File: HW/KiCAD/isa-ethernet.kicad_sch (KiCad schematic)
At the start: 42 parts, among them IC1 RTL8019AS, J5 IO-ADDR, J6 CONFIG, J7 CONFIG, J8 RJ45_LED_Shielded, U5 93LCxxB, Y2 20MHz

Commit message: some edit
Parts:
- IC1: footprint RTL8019AS:RTL8019AS -> Library:RTL8019AS
- J8: footprint Connector_RJ:RJ45_Bel_SI-60062-F -> Connector_RJ:RJ45_Cetus_J1B1211CCD_Horizontal
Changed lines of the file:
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@@
 			)
 		)
-		(property "Footprint" "Connector_RJ:RJ45_Bel_SI-60062-F"
+		(property "Footprint" "Connector_RJ:RJ45_Cetus_J1B1211CCD_Horizontal"
 			(at 259.08 33.655 90)
 			(effects
@@
 			)
 		)
-		(property "Footprint" "RTL8019AS:RTL8019AS"
+		(property "Footprint" "Library:RTL8019AS"
 			(at 152.4 101.6 0)
 			(effects

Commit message: some eidts, remove com
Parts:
- IC1: footprint Library:RTL8019AS -> kharon:RTL8019AS
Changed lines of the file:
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@@
 			)
 		)
-		(property "Footprint" "Library:RTL8019AS"
+		(property "Footprint" "kharon:RTL8019AS"
 			(at 152.4 101.6 0)
 			(effects

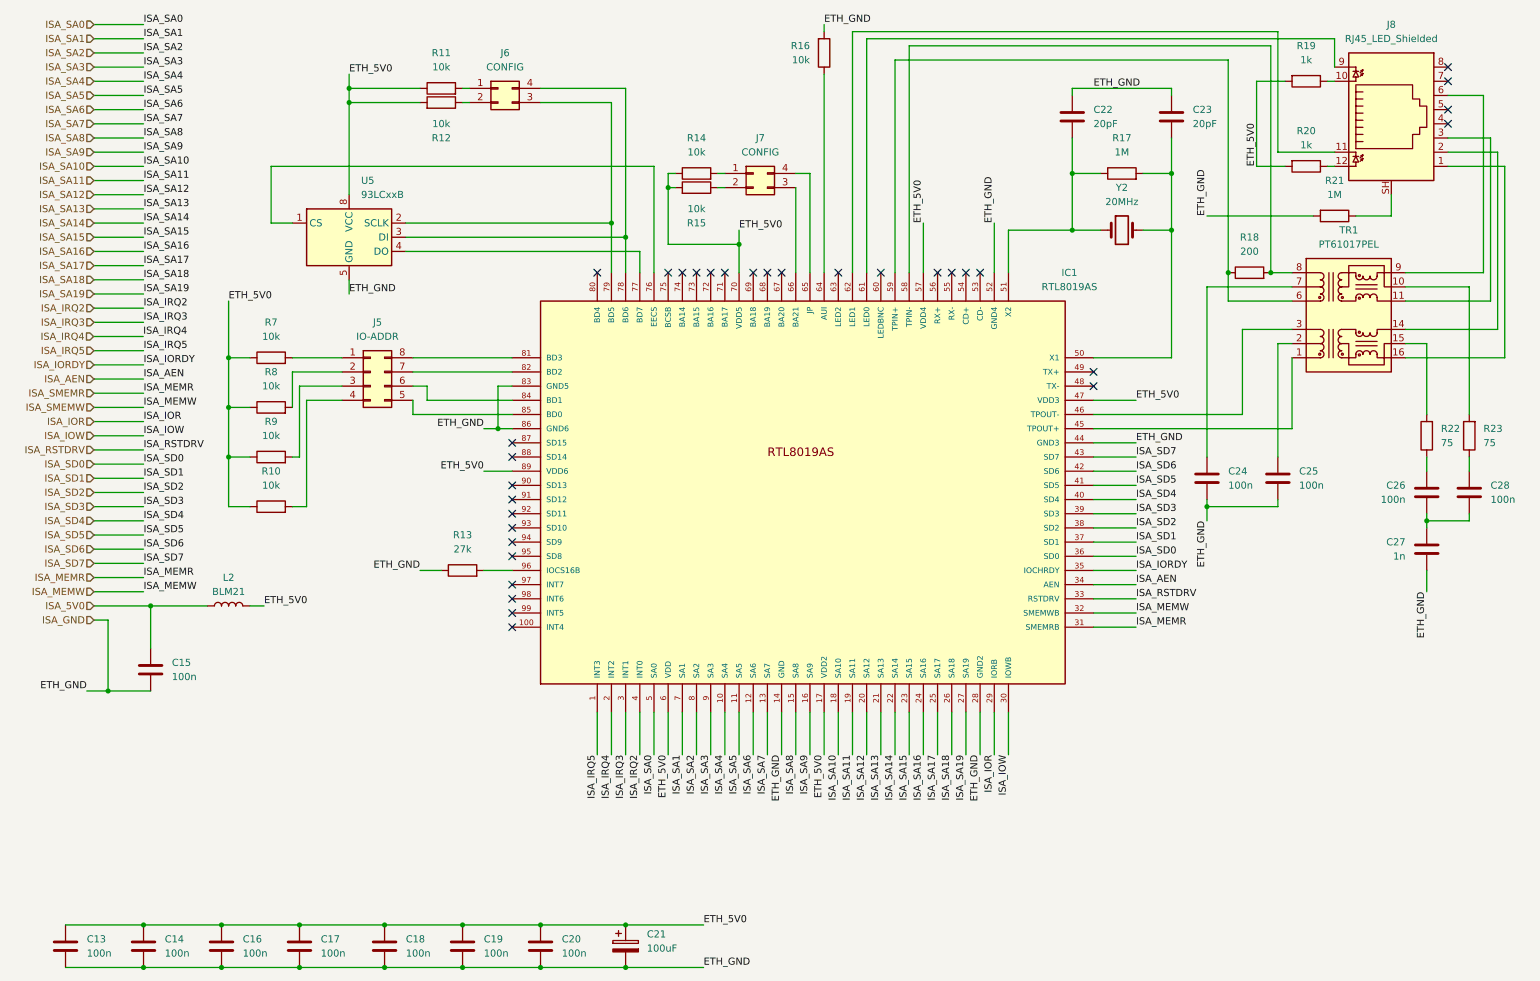
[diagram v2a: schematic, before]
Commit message: some edits, add HP amp
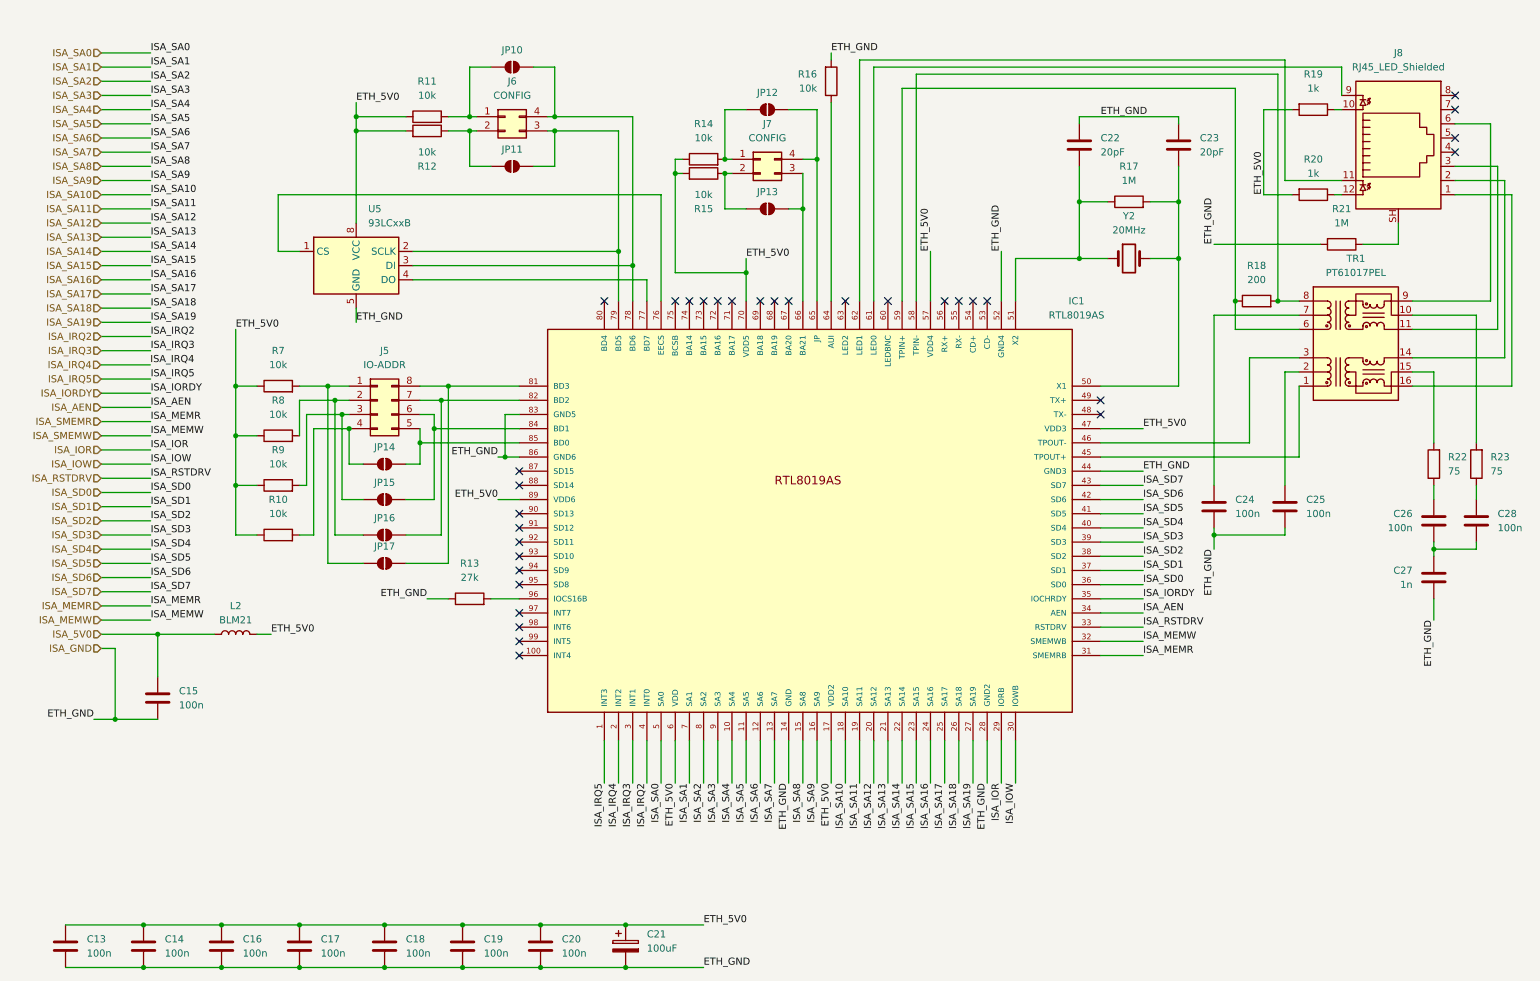
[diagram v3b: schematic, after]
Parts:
- added JP10, JP11, JP12, JP13, JP14, JP15, JP16, JP17: ~, Jumper:SolderJumper-2_P1.3mm_Open_TrianglePad1.0x1.5mm, symbol Jumper:SolderJumper_2_Open
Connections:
- net at J5.1 (Pin_1), R7.2: now also JP17.1 (A)
- net at J5.2 (Pin_2), R8.2: now also JP16.1 (A)
- net at J5.3 (Pin_3), R9.2: now also JP15.1 (A)
- net at J5.4 (Pin_4), R10.2: now also JP14.1 (A)
- net at IC1.85 (BD0), J5.5 (Pin_5): now also JP14.2 (B)
- net at IC1.84 (BD1), J5.6 (Pin_6): now also JP15.2 (B)
- net at IC1.82 (BD2), J5.7 (Pin_7): now also JP16.2 (B)
- net at IC1.81 (BD3), J5.8 (Pin_8): now also JP17.2 (B)
- net at J6.1 (Pin_1), R11.2: now also JP10.1 (A)
- net at J6.2 (Pin_2), R12.1: now also JP11.1 (A)
- net at IC1.79 (BD5), J6.3 (Pin_3), U5.2 (SCLK): now also JP11.2 (B)
- net at IC1.78 (BD6), J6.4 (Pin_4), U5.3 (DI): now also JP10.2 (B)
- net at J7.2 (Pin_2), R15.1: now also JP13.1 (A)
- net at J7.1 (Pin_1), R14.2: now also JP12.1 (A)
- net at IC1.65 (JP), J7.4 (Pin_4): now also JP12.2 (B)
- net at IC1.66 (BA21), J7.3 (Pin_3): now also JP13.2 (B)
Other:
- moved on the sheet: C15, C22, C23, C24, C25, C26, C27, C28, IC1, J5, J6, J7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
